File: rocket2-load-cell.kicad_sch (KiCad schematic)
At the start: 36 parts, among them J1 SWD, J2 Screw_Terminal_01x02, U2 STM32F103C8Tx, U3 AMS1117-3.3, Y1 16MHz

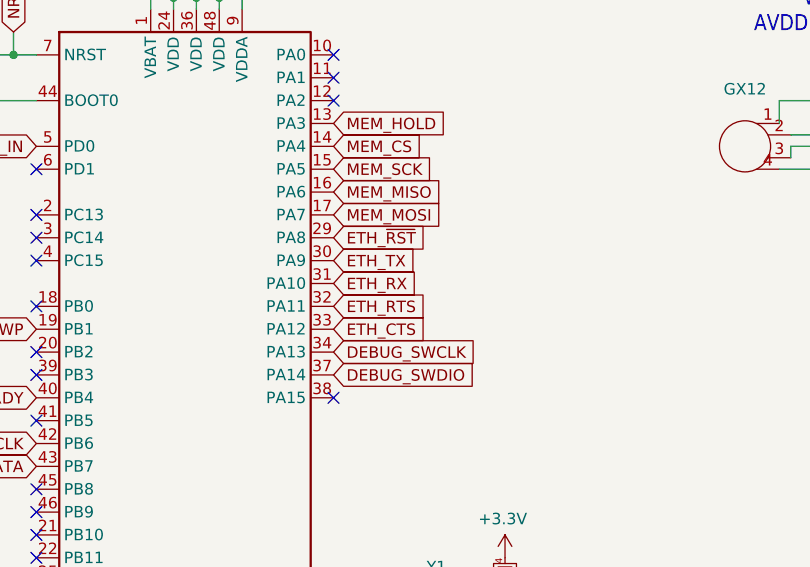
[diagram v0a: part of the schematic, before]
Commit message: made it so that all vias are connected, should be good for fabrication, no design errors now
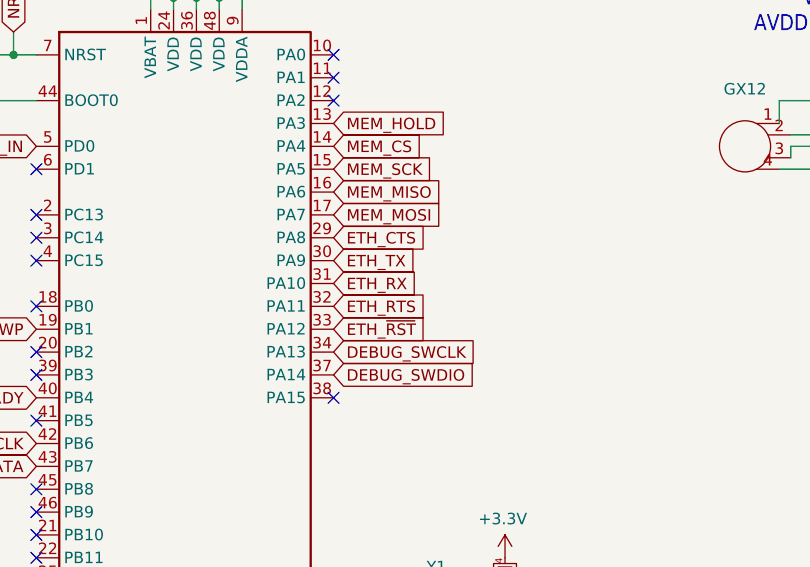
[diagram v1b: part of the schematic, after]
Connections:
- net ETH_CTS: now also U2.29 (PA8); no longer U2.33 (PA12)
- net ETH_~{RST}: now also U2.33 (PA12); no longer U2.29 (PA8)

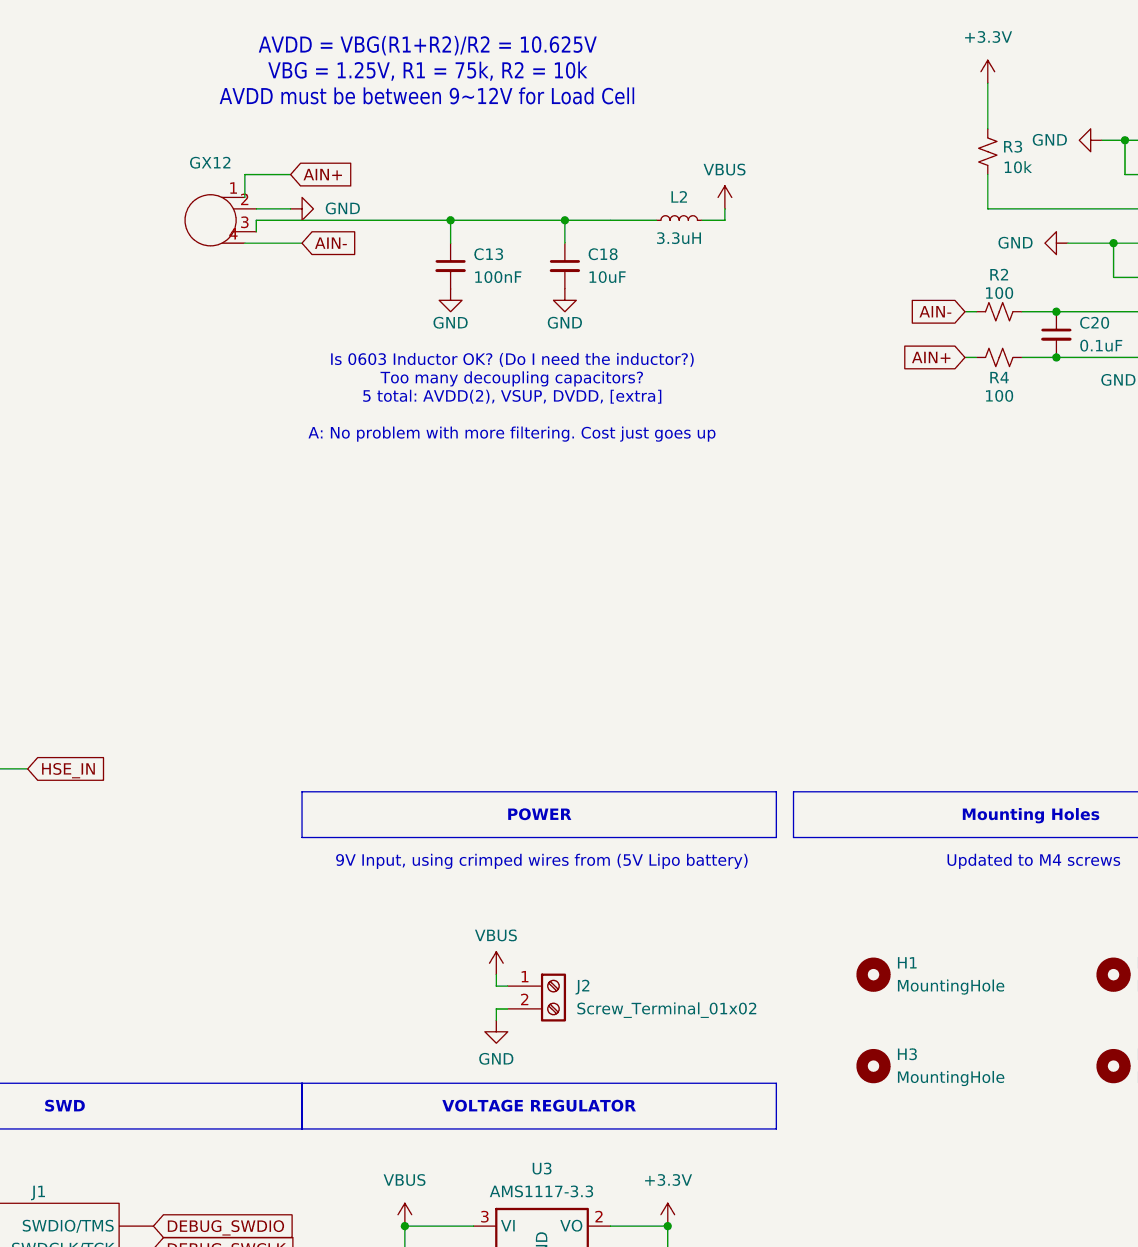
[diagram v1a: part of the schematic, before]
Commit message: added gx12 connector and fixed varioius other design problems
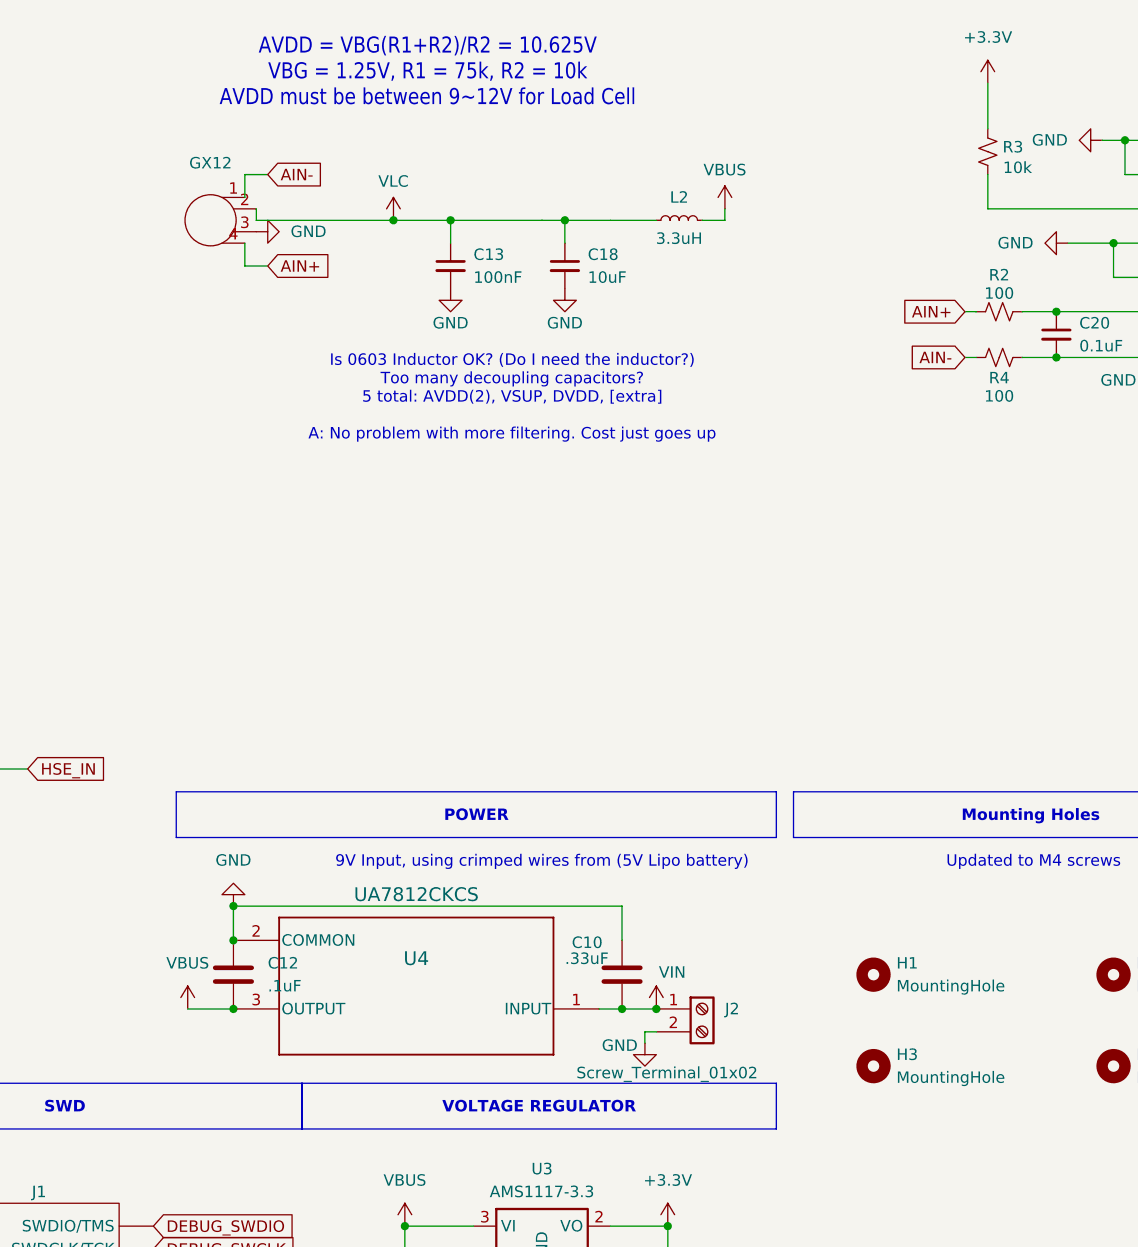
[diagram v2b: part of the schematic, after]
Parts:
- added C10: .33uF, Capacitor_SMD:C_0603_1608Metric, symbol Device:C
- added C12: .1uF, Capacitor_SMD:C_0603_1608Metric, symbol Device:C
- added U4: UA7812CKCS, KCS0003B, symbol UCIRP-LoadCell:UA7812CKCS
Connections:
- net AIN+: now also GX12.4, R2.1; no longer GX12.1, R4.1
- net AIN-: now also GX12.1, R4.1; no longer GX12.4, R2.1
- net GND: now also GX12.3, C10.1, C12.1, U4.2 (COMMON); no longer GX12.2
- net VBUS: now also C12.2, U4.3 (OUTPUT); no longer J2.1 (Pin_1)
- net VLC: now reaches C13.1, C18.1, L2.1
- net VLC: now also GX12.2; no longer GX12.3
- new net VIN: C10.2, J2.1 (Pin_1), U4.1 (INPUT)
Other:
- moved on the sheet: J2

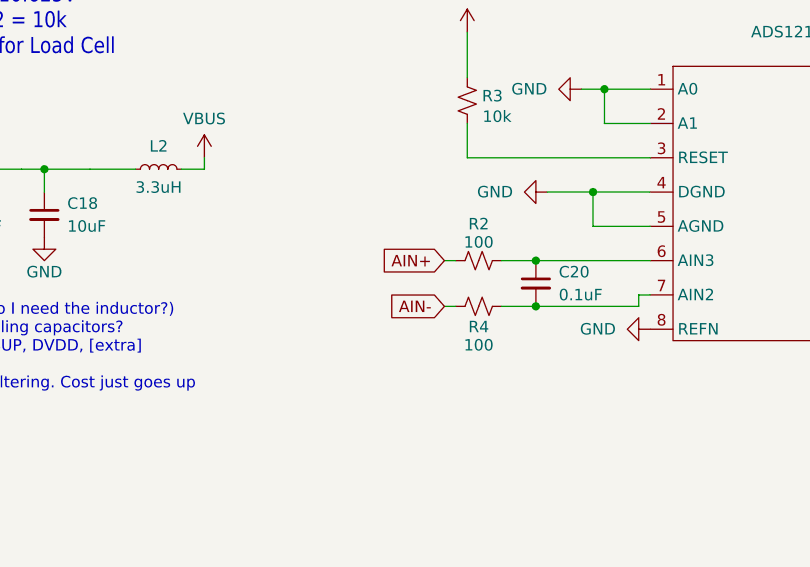
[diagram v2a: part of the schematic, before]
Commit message: added cad models to board
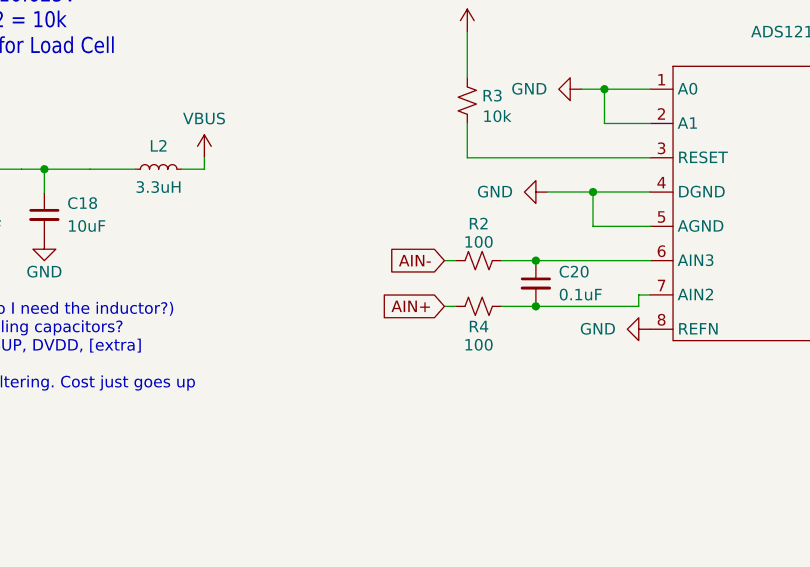
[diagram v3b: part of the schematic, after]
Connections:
- net AIN+: now also R4.1; no longer R2.1
- net AIN-: now also R2.1; no longer R4.1
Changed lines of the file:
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@@
-	(wire
-		(pts
-			(xy 195.58 81.28) (xy 196.85 81.28)
-		)
-		(stroke
-			(width 0)
-			(type default)
-		)
-	)
 	(wire
 		(pts
@@
 	(wire
 		(pts
+			(xy 195.58 81.28) (xy 196.85 81.28)
+		)
+		(stroke
+			(width 0)
+			(type default)
+		)
+	)
+	(wire
+		(pts
 			(xy 53.34 49.53) (xy 53.34 50.8)
 		)
@@
 	(wire
 		(pts
+			(xy 195.58 76.2) (xy 196.85 76.2)
+		)
+		(stroke
+			(width 0)
+			(type default)
+		)
+	)
+	(wire
+		(pts
 			(xy 49.53 130.81) (xy 49.53 132.08)
 		)
@@
 		(pts
 			(xy 48.26 129.54) (xy 48.26 130.81)
-		)
-		(stroke
-			(width 0)
-			(type default)
-		)
-	)
-	(wire
-		(pts
-			(xy 195.58 76.2) (xy 196.85 76.2)
 		)
 		(stroke
@@
 	(global_label "AIN+"
 		(shape input)
+		(at 195.58 81.28 180)
+		(fields_autoplaced yes)
+		(effects
+			(font
+				(size 1.27 1.27)
+			)
+			(justify right)
+		)
+		(property "Intersheetrefs" "${INTERSHEET_REFS}"
+			(at 187.9985 81.28 0)
+			(effects
+				(font
+					(size 1.27 1.27)
+				)
+				(justify right)
+				(hide yes)
+			)
+		)
+	)
+	(global_label "NRST"
+		(shape input)
+		(at 30.48 53.34 90)
+		(fields_autoplaced yes)
+		(effects
+			(font
+				(size 1.27 1.27)
+			)
+			(justify left)
+		)
+		(property "Intersheetrefs" "${INTERSHEET_REFS}"
+			(at 30.48 45.5772 90)
+			(effects
+				(font
+					(size 1.27 1.27)
+				)
+				(justify left)
+				(hide yes)
+			)
+		)
+	)
+	(global_label "AIN-"
+		(shape input)
 		(at 195.58 76.2 180)
 		(fields_autoplaced yes)
@@
 			(effects
 				(font
-					(size 1.27 1.27)
-				)
-				(justify right)
-				(hide yes)
-			)
-		)
-	)
-	(global_label "NRST"
-		(shape input)
-		(at 30.48 53.34 90)
-		(fields_autoplaced yes)
-		(effects
-			(font
-				(size 1.27 1.27)
-			)
-			(justify left)
-		)
-		(property "Intersheetrefs" "${INTERSHEET_REFS}"
-			(at 30.48 45.5772 90)
-			(effects
-				(font
-					(size 1.27 1.27)
-				)
-				(justify left)
-				(hide yes)
-			)
-		)
-	)
-	(global_label "AIN-"
-		(shape input)
-		(at 195.58 81.28 180)
-		(fields_autoplaced yes)
-		(effects
-			(font
-				(size 1.27 1.27)
-			)
-			(justify right)
-		)
-		(property "Intersheetrefs" "${INTERSHEET_REFS}"
-			(at 187.9985 81.28 0)
-			(effects
-				(font

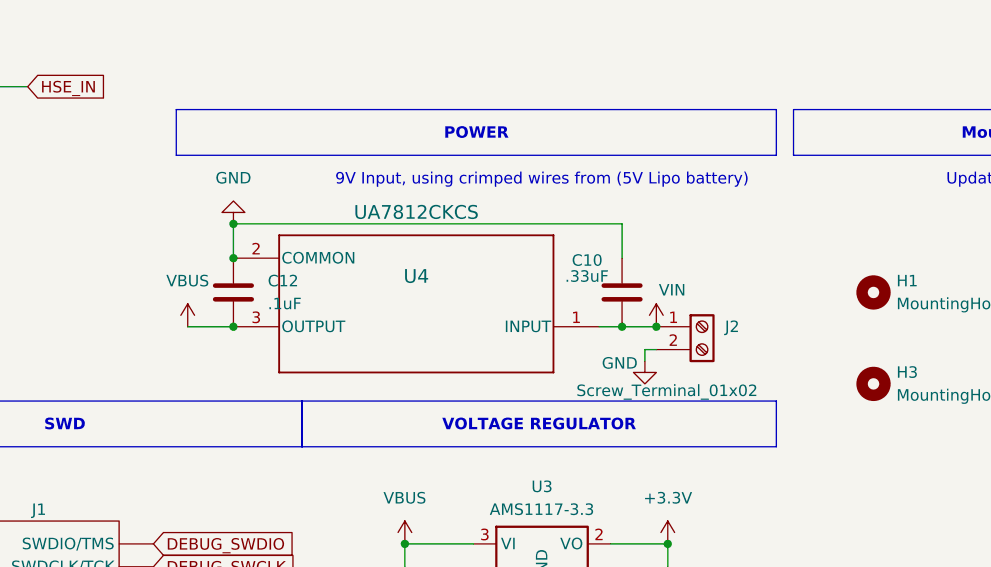
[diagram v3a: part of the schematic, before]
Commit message: changed back to 5v and removed 12 volt reg
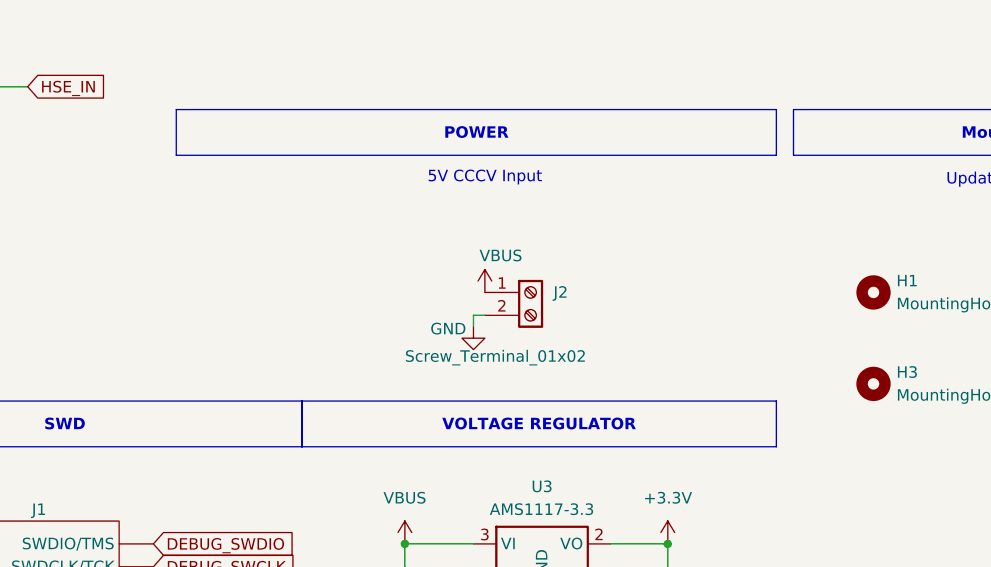
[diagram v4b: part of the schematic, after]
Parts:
- removed C10: .33uF, Capacitor_SMD:C_0603_1608Metric, symbol Device:C
- removed C12: .1uF, Capacitor_SMD:C_0603_1608Metric, symbol Device:C
- removed U4: UA7812CKCS, KCS0003B, symbol UCIRP-LoadCell:UA7812CKCS
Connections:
- net VIN is gone; now on net VBUS: J2.1 (Pin_1)
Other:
- note added: "5V CCCV Input"
- note removed: "9V Input, using crimped wires from (5V Lipo battery)"
- moved on the sheet: J2
